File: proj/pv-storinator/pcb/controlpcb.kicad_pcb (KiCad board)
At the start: 2 copper layers, 98 x 61.5 mm, 65 parts, among them J1 Conn_01x06_Socket, J10 Conn_01x01, J11 Conn_01x01, J12 Conn_01x06_Socket, J13 Conn_01x07_Socket, J14 Conn_01x01, J15 Conn_01x01, J16 Conn_01x04_Socket, J17 Conn_01x06_Socket, J18 Conn_01x01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

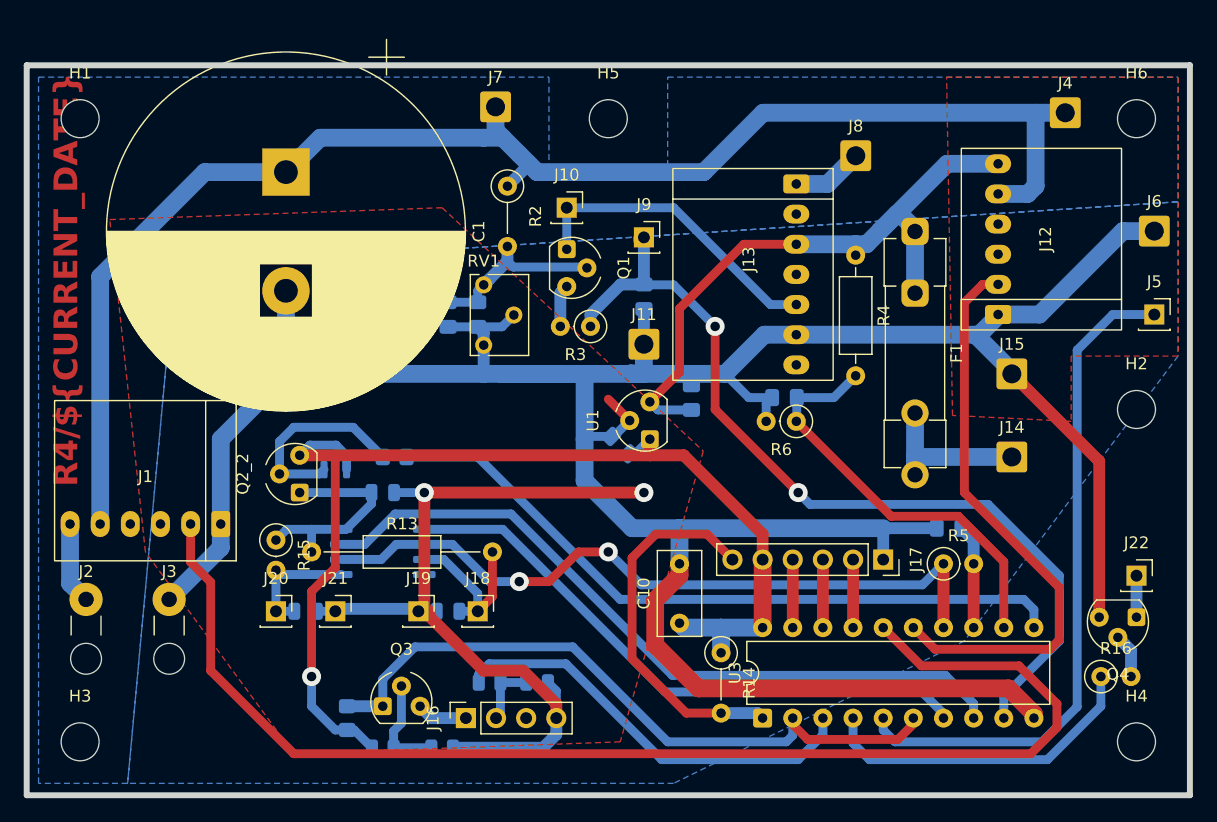
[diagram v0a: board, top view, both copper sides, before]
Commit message: pv-storinator: Improve mounting holes and R5 + R6 values
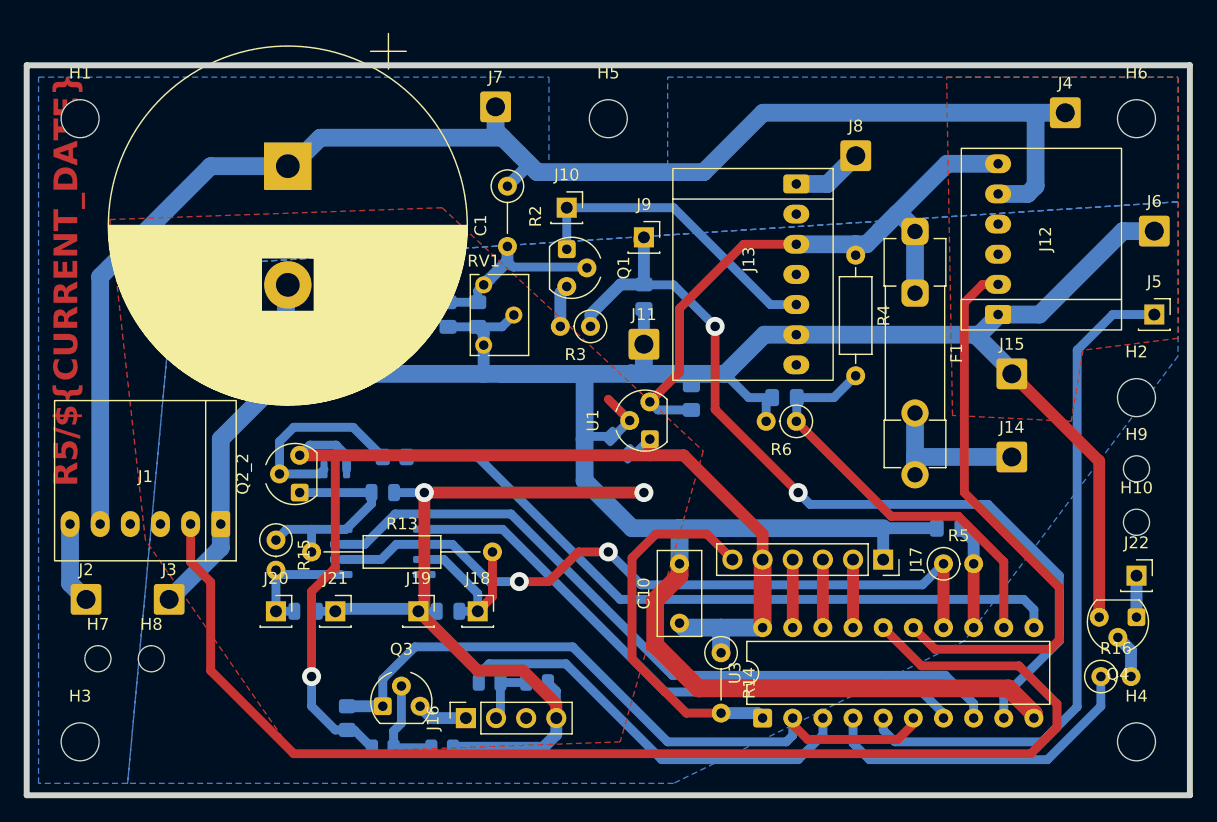
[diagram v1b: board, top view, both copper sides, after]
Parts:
- added H10: MountingHole, MountingHole:MountingHole_2.2mm_M2_DIN965, F.Cu at (148.5, 88.5)
- added H7: MountingHole, MountingHole:MountingHole_2.2mm_M2_DIN965, F.Cu at (61.0, 100.0)
- added H8: MountingHole, MountingHole:MountingHole_2.2mm_M2_DIN965, F.Cu at (65.5, 100.0)
- added H9: MountingHole, MountingHole:MountingHole_2.2mm_M2_DIN965, F.Cu at (148.5, 84.0)
- J2, J3: footprint Custom_Footprints:SolderWire_D1.3mm_OD2.6mm -> Connector_Wire:SolderWire-0.75sqmm_1x01_D1.25mm_OD2.3mm
- R5: value 100k -> 47k
- R6: value 68k -> 47k
- moved H2 1.00 mm to (148.5, 78.0)
- moved C1 0.52 mm to (77.0, 58.5)

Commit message: pv-storinator: Minor schematic improvements
- More efficient voltage regulator (lower quiescent current)
- SMD alternatives (hand soldering)
- Pull-Down on charge DC/DC for safety
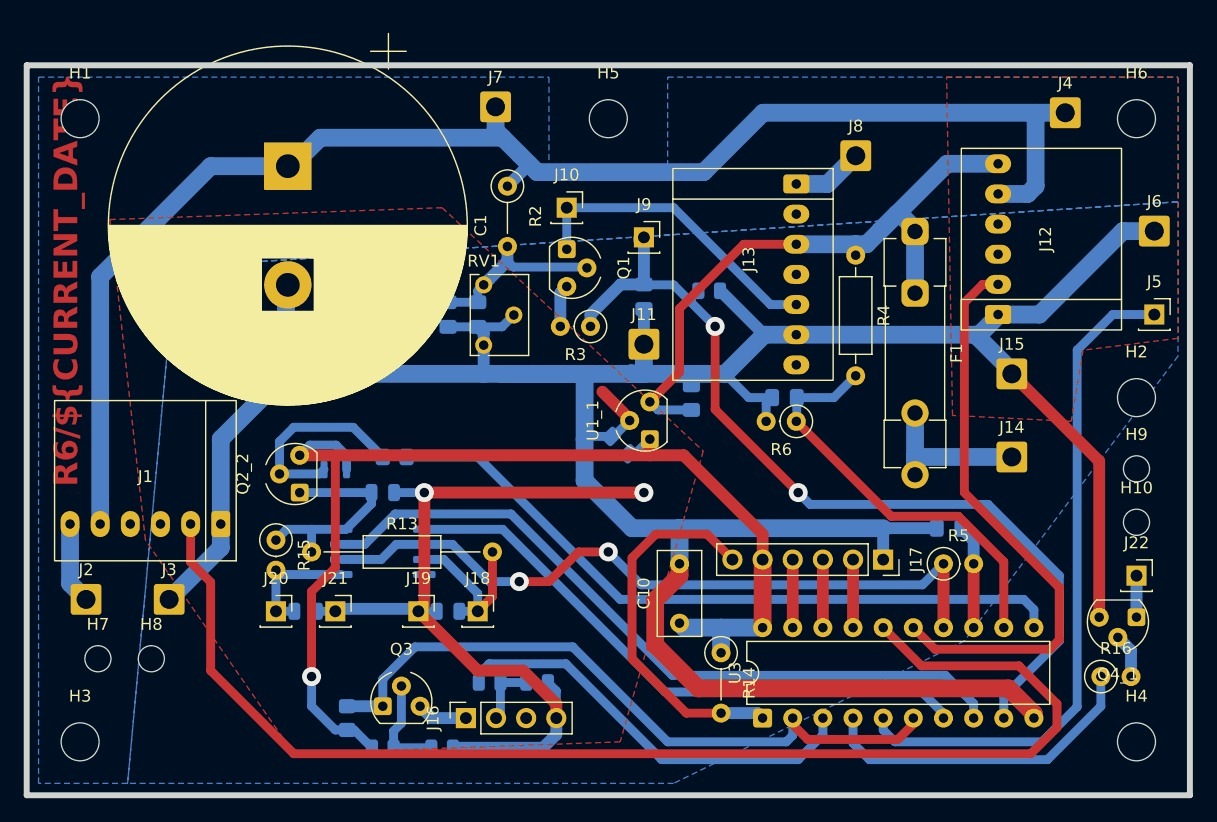
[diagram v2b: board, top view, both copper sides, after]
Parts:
- removed Q4: NPN, Custom_Footprints:TO-92_W
- removed U1: L78L05_TO92, Custom_Footprints:TO-92_W
- added Q4_1: NPN, Custom_Footprints:TO-92_W, F.Cu at (148.5, 96.5)
- added R1: 22k, Resistor_SMD:R_0805_2012Metric, B.Cu at (112.5, 69.0)
- added U1_1: AP7381-50V-A, Custom_Footprints:TO-92_W, F.Cu at (107.5, 81.5)
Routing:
- net GND: track 339.4 -> 345.3 mm
- net DCDC_EN: track 73.9 -> 75.1 mm

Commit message: pv-storinator: Improve PCB
- Fix incorrect MCU_PWM_0A connection
- Add TVS (suppressor) diode for safety
- Enlarge holes for easier cable mounting
- Add custom footprint library (previously missing)
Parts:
- removed Q2_1: Q_PMOS_GSD, Package_TO_SOT_SMD:SOT-23
- removed Q2_2: BC557, Custom_Footprints:TO-92_W
- removed Q4_1: NPN, Custom_Footprints:TO-92_W
- added D1: TVS 24V ... 30V, Diode_SMD:D_SMA-SMB_Universal_Handsoldering, B.Cu at (66.5, 92.5)
- added D2: LED red, LED_SMD:LED_0603_1608Metric, B.Cu at (116.0, 70.0)
- added Q2: SOT-23, Package_TO_SOT_SMD:SOT-23, B.Cu at (81.0, 85.0)
- added Q4: SOT-23(-3): BSS316N / PJA3432 / DMG3406L / ?, Package_TO_SOT_SMD:SOT-23-3, B.Cu at (148.5, 99.0)
- added R17: 0R, Resistor_SMD:R_0805_2012Metric_Pad1.20x1.40mm_HandSolder, B.Cu at (58.5, 93.5)
- H10, H7, H8, H9: footprint MountingHole:MountingHole_2.2mm_M2_DIN965 -> MountingHole:MountingHole_2.5mm
- J1, J12: footprint Custom_Symbols:SIP-6_Upright_Board -> Custom_Footprints:SIP-6_Upright_Board
- J10, J5, J9: footprint Connector_PinSocket_2.54mm:PinSocket_1x01_P2.54mm_Vertical -> Connector_Wire:SolderWire-0.5sqmm_1x01_D0.9mm_OD2.1mm
- J13: footprint Custom_Symbols:SIP-7_Upright_Board -> Custom_Footprints:SIP-7_Upright_Board
- J18, J19, J20, J21: footprint Connector_PinSocket_2.54mm:PinSocket_1x01_P2.54mm_Vertical -> Connector_PinHeader_2.54mm:PinHeader_1x01_P2.54mm_Vertical
- J22: value Conn_01x01 -> Pin header; footprint Connector_PinSocket_2.54mm:PinSocket_1x01_P2.54mm_Vertical -> Connector_PinHeader_2.54mm:PinHeader_1x02_P2.54mm_Vertical
- R16: value 3.3k -> 10k; footprint Resistor_THT:R_Axial_DIN0207_L6.3mm_D2.5mm_P2.54mm_Vertical -> Resistor_SMD:R_0805_2012Metric_Pad1.20x1.40mm_HandSolder; moved to B.Cu
- R9: value 27k -> 10k
- moved J22 3.04 mm to (149.0, 96.0), turned to 180 degrees
- moved H2 1.50 mm to (148.5, 76.5)
- moved H8 1.41 mm to (66.5, 101.0)
- moved H9 1.41 mm to (147.5, 83.0)
- moved H7 1.12 mm to (60.5, 101.0)
- moved J2 1.12 mm to (60.5, 96.0)
- moved H10 1.00 mm to (147.5, 88.5)
- moved J3 1.00 mm to (67.0, 96.0)
- moved R16 0.50 mm to (145.5, 102.0), turned to 90 degrees
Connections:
- J2 pad 1: /Vin -> Net-(J2-Pin_1)
- U2 pad 2: MCU_PWM_0A -> PWM_0A_DC
- U2 pad 6: MCU_PWM_0A -> PWM_0A_DC
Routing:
- net PWM_0A_DC: track 8.81 -> 66.8 mm, vias 0 -> 2
- net MCU_PWM_0A: track 60.9 -> 5.38 mm, vias 2 -> 0
- net GND: track 345.3 -> 349.8 mm, vias 2 -> 3
- net /V_OPAMP: track 18.2 -> 15.2 mm
- net Net-(J2-Pin_1): track 0.00 -> 2.62 mm
- net /Vin: track 6.91 -> 9.01 mm
- net FAN_EN: track 27.9 -> 26.4 mm
- net Net-(Q4-G): track 3.76 -> 2.30 mm
- net +5V: vias 1 -> 2
